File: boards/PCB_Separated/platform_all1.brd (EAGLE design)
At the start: 8.3 x 2 mm, 80 parts, among them IC1 FT232RL, IC2 7805DT, IC3 7805DT, U1 STM32F10XRXT6, X1 32khz, X2 8mhz, X3 MINI-USB_SHIELD5P2-32005-601

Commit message: revisi driver
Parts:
- moved C-VCC 1.27 mm to (41.9, 8.89)
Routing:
- net VSS: track 362.0 -> 363.3 mm
- net V12: track 166.3 -> 167.0 mm
- net VCC: track 178.2 -> 178.7 mm
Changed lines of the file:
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@@
 <element name="C-V12" library="resistor" package="PANASONIC_D" value="100u/25v" x="60.96" y="7.62" rot="MR270"/>
 <element name="D-V12" library="diode" package="SMB" value="" x="58.42" y="15.24" rot="MR270"/>
-<element name="C-VCC" library="resistor" package="PANASONIC_D" value="100u/25v" x="43.18" y="8.89" rot="MR270"/>
+<element name="C-VCC" library="resistor" package="PANASONIC_D" value="100u/25v" x="41.91" y="8.89" rot="MR270"/>
 <element name="OK-INJ" library="optocoupler" package="DIL04" value="PC817" x="26.67" y="55.88" rot="R90">
 <attribute name="OC_NEWARK" value="97K7059" x="66.04" y="83.82" size="1.778" layer="27" rot="R90" display="off"/>
@@
 <wire x1="48.26" y1="21.59" x2="49.53" y2="22.86" width="0.6096" layer="16"/>
 <wire x1="49.53" y1="22.86" x2="49.6062" y2="22.86" width="0.6096" layer="16"/>
-<wire x1="43.18" y1="11.29" x2="43.18" y2="12.7" width="0.6096" layer="16"/>
-<wire x1="43.18" y1="12.7" x2="48.26" y2="12.7" width="0.6096" layer="16"/>
 <wire x1="48.26" y1="12.7" x2="48.895" y2="13.335" width="0.6096" layer="16"/>
 <wire x1="59.13" y1="46.37" x2="59.13" y2="45.01" width="0.3048" layer="16"/>
@@
 <wire x1="38.1" y1="74.93" x2="33.02" y2="69.85" width="0.3048" layer="16"/>
 <wire x1="33.02" y1="69.85" x2="33.02" y2="68.58" width="0.3048" layer="16"/>
+<wire x1="48.26" y1="12.7" x2="41.91" y2="12.7" width="0.6096" layer="16"/>
+<wire x1="41.91" y1="12.7" x2="41.91" y2="11.29" width="0.6096" layer="16"/>
 </signal>
 <signal name="VDD">
@@
 <contactref element="ANALOG" pad="1"/>
 <wire x1="45.88" y1="11.29" x2="46" y2="11.17" width="0.6096" layer="16"/>
-<wire x1="43.18" y1="6.49" x2="43.18" y2="7.62" width="0.6096" layer="16"/>
-<wire x1="43.18" y1="7.62" x2="44.45" y2="8.89" width="0.6096" layer="16"/>
+<wire x1="41.91" y1="6.49" x2="43.18" y2="7.62" width="0.6096" layer="16"/>
 <wire x1="44.45" y1="8.89" x2="45.72" y2="8.89" width="0.6096" layer="16"/>
 <wire x1="45.72" y1="8.89" x2="45.72" y2="10.89" width="0.6096" layer="16"/>
@@
 <wire x1="82.55" y1="52.07" x2="81.5594" y2="52.07" width="0.6096" layer="16"/>
 <wire x1="81.5594" y1="52.07" x2="81.28" y2="51.7906" width="0.6096" layer="16"/>
+<wire x1="44.45" y1="8.89" x2="43.18" y2="7.62" width="0.6096" layer="16"/>
 </signal>
 <signal name="DP">
@@
 <wire x1="46.99" y1="3.81" x2="46.99" y2="5.08" width="0.6096" layer="16"/>
 <wire x1="46.99" y1="5.08" x2="47.26" y2="5.35" width="0.6096" layer="16"/>
-<wire x1="46" y1="14.23" x2="42.17" y2="14.23" width="0.6096" layer="16"/>
-<wire x1="42.17" y1="14.23" x2="39.37" y2="11.43" width="0.6096" layer="16"/>
-<wire x1="39.37" y1="11.43" x2="39.37" y2="5.08" width="0.6096" layer="16"/>
+<wire x1="46" y1="14.23" x2="40.9" y2="14.23" width="0.6096" layer="16"/>
+<wire x1="39.37" y1="12.7" x2="39.37" y2="5.08" width="0.6096" layer="16"/>
 <wire x1="39.37" y1="5.08" x2="38.1" y2="3.81" width="0.6096" layer="16"/>
 <wire x1="60.96" y1="5.22" x2="60.96" y2="3.81" width="0.6096" layer="16"/>
@@
 <wire x1="13.97" y1="38.1" x2="15.088" y2="38.1" width="0.6096" layer="16"/>
 <wire x1="15.088" y1="38.1" x2="15.24" y2="38.252" width="0.6096" layer="16"/>
+<wire x1="39.37" y1="12.7" x2="40.9" y2="14.23" width="0.6096" layer="16"/>
 </signal>
 <signal name="INJ">

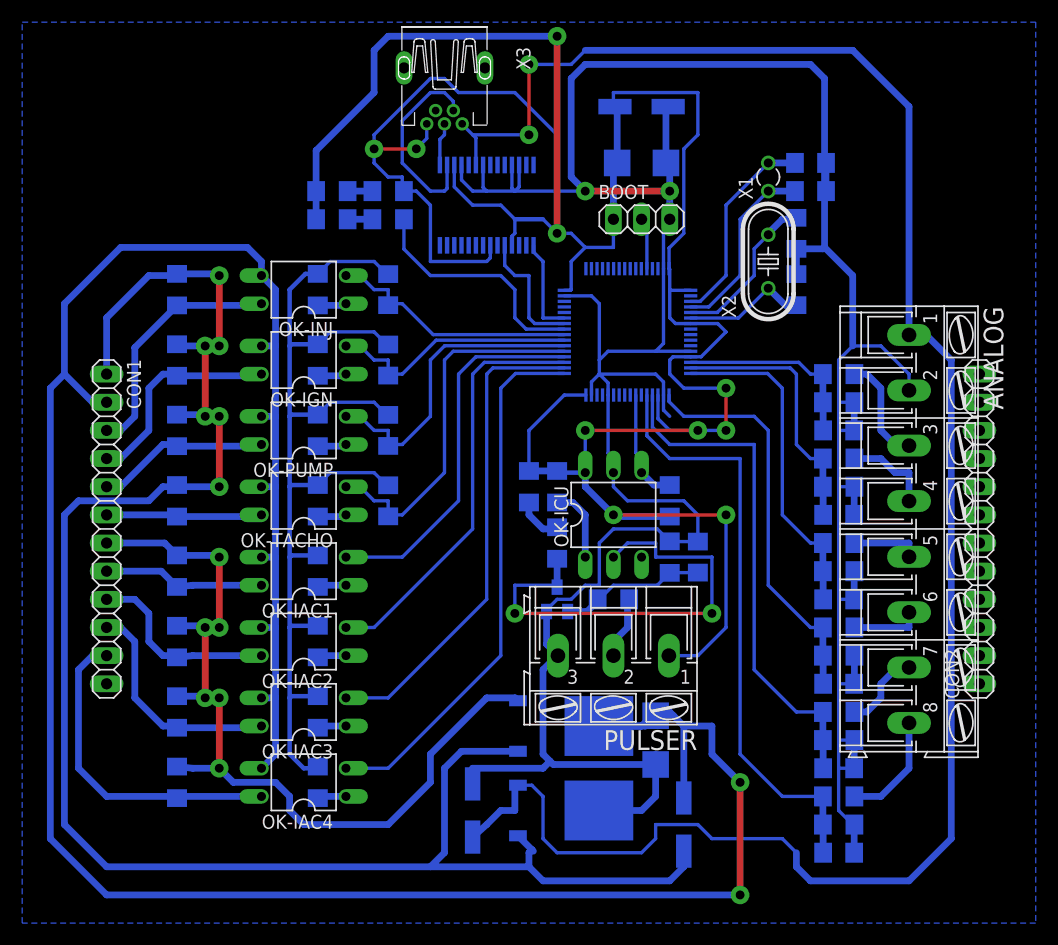
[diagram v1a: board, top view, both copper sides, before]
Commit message: edit mini usb and deactivate delayed startup
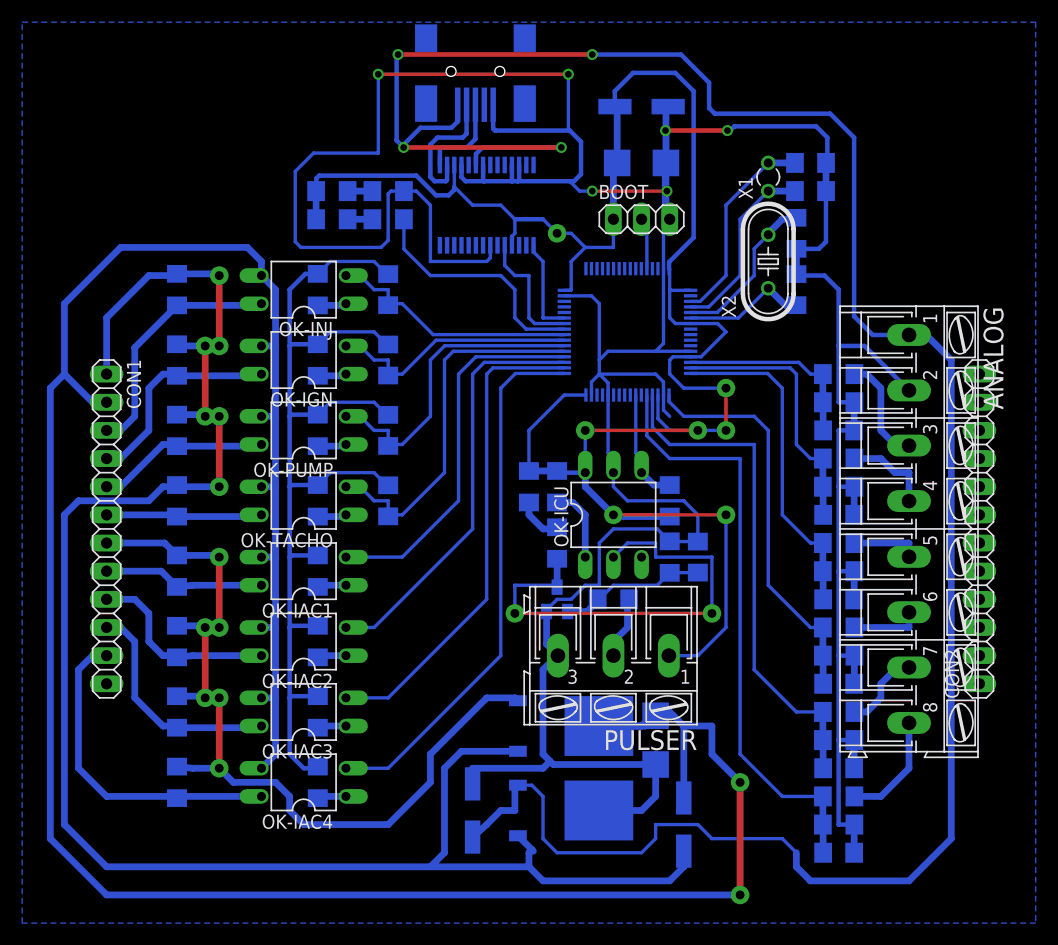
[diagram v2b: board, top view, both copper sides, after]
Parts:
- removed X3: MINI-USB_SHIELD5P2-32005-601, con-cypressindustries:32005-601
- added USB: MINI-USB-32005-201, con-cypressindustries:32005-201
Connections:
- net DM: now also USB.2; no longer X3.2
- net DP: now also USB.3; no longer X3.3
- net VCC: now also USB.1; no longer X3.1
- net VSS: now also USB.5; no longer X3.5
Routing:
- net VDD: track 221.7 -> 187.8 mm, vias 8 -> 7
- net VCC: track 178.7 -> 212.4 mm, vias 2 -> 4
- net VSS: track 363.3 -> 373.7 mm, vias 4 -> 6
- net DM: track 17.9 -> 12.3 mm
- net DP: track 3.88 -> 8.18 mm
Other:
- board outline removed
